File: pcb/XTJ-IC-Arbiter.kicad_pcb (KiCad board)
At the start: 2 copper layers, 82.1 x 48.1 mm, 33 parts, among them J3 DTM13-12PA-R008, SW2 SW_DIP_x02, U1 LM2672N-5.0, U3 Teensy4.0, U4 MCP2562-H-P, U5 SP723ABG

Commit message: 3.3v conn
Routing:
- net 3v3: track 9.27 -> 53.9 mm
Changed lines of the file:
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@@
       (net 4 "can+") (pinfunction "12") (pintype "passive"))
     (model "${KIPRJMOD}/parts/DTM13/DTM13-12PA-R008.step"
-      (offset (xyz 0.635 -30.48 8.255))
+      (offset (xyz 0 -30.48 8.255))
       (scale (xyz 1 1 1))
       (rotate (xyz -90 0 0))
@@
   (segment (start 103.9638 106.7292) (end 103.9638 105.021384) (width 0.1524) (layer "F.Cu") (net 17))
   (segment (start 91.821 108.585) (end 89.027 111.379) (width 0.5) (layer "F.Cu") (net 18))
+  (segment (start 93.8038 105.798616) (end 93.8038 105.021384) (width 0.1524) (layer "F.Cu") (net 20))
+  (segment (start 119.2038 104.4718) (end 120.142 105.41) (width 0.1524) (layer "F.Cu") (net 20))
+  (segment (start 91.458813 112.306) (end 92.437187 112.306) (width 0.1524) (layer "F.Cu") (net 20))
+  (segment (start 87.628 114.504) (end 90.767 111.365) (width 0.1524) (layer "F.Cu") (net 20))
+  (segment (start 110.4498 106.3482) (end 111.5838 105.2142) (width 0.1524) (layer "F.Cu") (net 20))
+  (segment (start 92.437187 112.306) (end 94.71 110.033187) (width 0.1524) (layer "F.Cu") (net 20))
+  (segment (start 112.133384 104.4718) (end 119.2038 104.4718) (width 0.1524) (layer "F.Cu") (net 20))
+  (segment (start 94.665784 104.1594) (end 108.2896 104.1594) (width 0.1524) (layer "F.Cu") (net 20))
   (segment (start 117.71 113.646) (end 117.729 113.665) (width 0.1524) (layer "F.Cu") (net 20))
+  (segment (start 108.2896 104.1594) (end 109.0438 104.9136) (width 0.1524) (layer "F.Cu") (net 20))
+  (segment (start 90.767 111.614187) (end 91.458813 112.306) (width 0.1524) (layer "F.Cu") (net 20))
+  (segment (start 94.71 110.033187) (end 94.71 106.704816) (width 0.1524) (layer "F.Cu") (net 20))
+  (segment (start 111.5838 105.2142) (end 111.5838 105.021384) (width 0.1524) (layer "F.Cu") (net 20))
+  (segment (start 111.5838 105.021384) (end 112.133384 104.4718) (width 0.1524) (layer "F.Cu") (net 20))
+  (segment (start 109.0438 105.798616) (end 109.593384 106.3482) (width 0.1524) (layer "F.Cu") (net 20))
+  (segment (start 90.767 111.365) (end 90.767 111.614187) (width 0.1524) (layer "F.Cu") (net 20))
+  (segment (start 94.71 106.704816) (end 93.8038 105.798616) (width 0.1524) (layer "F.Cu") (net 20))
+  (segment (start 109.593384 106.3482) (end 110.4498 106.3482) (width 0.1524) (layer "F.Cu") (net 20))
   (segment (start 117.71 110.838) (end 117.71 113.646) (width 0.1524) (layer "F.Cu") (net 20))
+  (segment (start 93.8038 105.021384) (end 94.665784 104.1594) (width 0.1524) (layer "F.Cu") (net 20))
+  (segment (start 109.0438 104.9136) (end 109.0438 105.798616) (width 0.1524) (layer "F.Cu") (net 20))
   (segment (start 120.142 108.406) (end 120.142 105.41) (width 0.1524) (layer "B.Cu") (net 20))
   (segment (start 117.71 110.838) (end 120.142 108.406) (width 0.1524) (layer "B.Cu") (net 20))

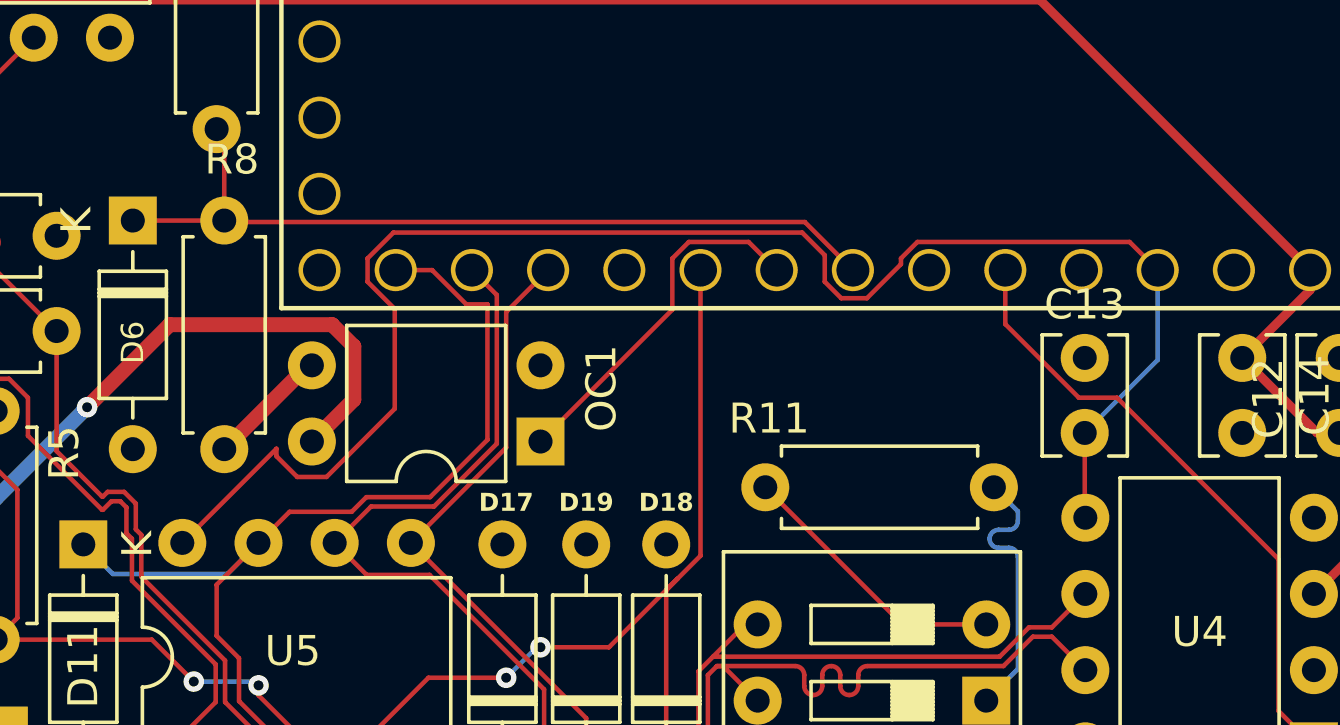
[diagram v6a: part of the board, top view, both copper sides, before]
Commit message: safer 3.3v trace
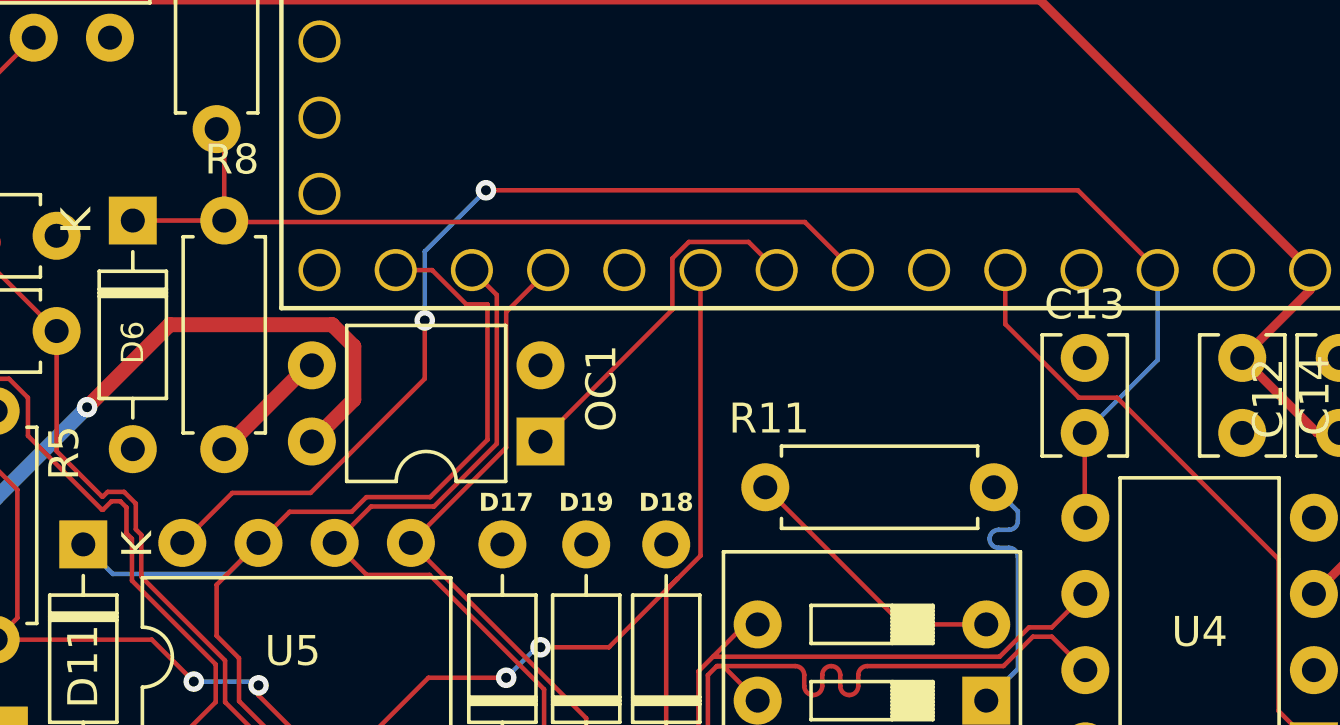
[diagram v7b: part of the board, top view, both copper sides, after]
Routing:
- net 3v3: track 53.9 -> 50.2 mm, vias 0 -> 2
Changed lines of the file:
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@@
     (pad_to_mask_clearance 0.0508)
     (solder_mask_min_width 0.1016)
-    (grid_origin 60.96 100.838)
     (pcbplotparams
       (layerselection 0x00010f0_ffffffff)
@@
   (segment (start 103.9638 106.7292) (end 103.9638 105.021384) (width 0.1524) (layer "F.Cu") (net 17))
   (segment (start 91.821 108.585) (end 89.027 111.379) (width 0.5) (layer "F.Cu") (net 18))
-  (segment (start 93.8038 105.798616) (end 93.8038 105.021384) (width 0.1524) (layer "F.Cu") (net 20))
-  (segment (start 119.2038 104.4718) (end 120.142 105.41) (width 0.1524) (layer "F.Cu") (net 20))
-  (segment (start 91.458813 112.306) (end 92.437187 112.306) (width 0.1524) (layer "F.Cu") (net 20))
-  (segment (start 87.628 114.504) (end 90.767 111.365) (width 0.1524) (layer "F.Cu") (net 20))
-  (segment (start 110.4498 106.3482) (end 111.5838 105.2142) (width 0.1524) (layer "F.Cu") (net 20))
-  (segment (start 92.437187 112.306) (end 94.71 110.033187) (width 0.1524) (layer "F.Cu") (net 20))
-  (segment (start 112.133384 104.4718) (end 119.2038 104.4718) (width 0.1524) (layer "F.Cu") (net 20))
-  (segment (start 94.665784 104.1594) (end 108.2896 104.1594) (width 0.1524) (layer "F.Cu") (net 20))
+  (segment (start 117.482 102.75) (end 120.142 105.41) (width 0.1524) (layer "F.Cu") (net 20))
   (segment (start 117.71 113.646) (end 117.729 113.665) (width 0.1524) (layer "F.Cu") (net 20))
-  (segment (start 108.2896 104.1594) (end 109.0438 104.9136) (width 0.1524) (layer "F.Cu") (net 20))
-  (segment (start 90.767 111.614187) (end 91.458813 112.306) (width 0.1524) (layer "F.Cu") (net 20))
-  (segment (start 94.71 110.033187) (end 94.71 106.704816) (width 0.1524) (layer "F.Cu") (net 20))
-  (segment (start 111.5838 105.2142) (end 111.5838 105.021384) (width 0.1524) (layer "F.Cu") (net 20))
-  (segment (start 111.5838 105.021384) (end 112.133384 104.4718) (width 0.1524) (layer "F.Cu") (net 20))
-  (segment (start 109.0438 105.798616) (end 109.593384 106.3482) (width 0.1524) (layer "F.Cu") (net 20))
-  (segment (start 90.767 111.365) (end 90.767 111.614187) (width 0.1524) (layer "F.Cu") (net 20))
-  (segment (start 94.71 106.704816) (end 93.8038 105.798616) (width 0.1524) (layer "F.Cu") (net 20))
-  (segment (start 109.593384 106.3482) (end 110.4498 106.3482) (width 0.1524) (layer "F.Cu") (net 20))
+  (segment (start 91.905187 112.838) (end 95.71 109.033187) (width 0.1524) (layer "F.Cu") (net 20))
+  (segment (start 95.71 109.033187) (end 95.71 107.088) (width 0.1524) (layer "F.Cu") (net 20))
+  (segment (start 97.75 102.75) (end 117.482 102.75) (width 0.1524) (layer "F.Cu") (net 20))
+  (segment (start 89.294 112.838) (end 91.905187 112.838) (width 0.1524) (layer "F.Cu") (net 20))
   (segment (start 117.71 110.838) (end 117.71 113.646) (width 0.1524) (layer "F.Cu") (net 20))
-  (segment (start 93.8038 105.021384) (end 94.665784 104.1594) (width 0.1524) (layer "F.Cu") (net 20))
-  (segment (start 109.0438 104.9136) (end 109.0438 105.798616) (width 0.1524) (layer "F.Cu") (net 20))
+  (segment (start 87.628 114.504) (end 89.294 112.838) (width 0.1524) (layer "F.Cu") (net 20))
+  (via (at 95.71 107.088) (size 0.6858) (drill 0.3302) (layers "F.Cu" "B.Cu") (net 20))
+  (via (at 97.75 102.75) (size 0.6858) (drill 0.3302) (layers "F.Cu" "B.Cu") (net 20))
   (segment (start 120.142 108.406) (end 120.142 105.41) (width 0.1524) (layer "B.Cu") (net 20))
+  (segment (start 95.71 104.79) (end 97.75 102.75) (width 0.1524) (layer "B.Cu") (net 20))
+  (segment (start 95.71 107.088) (end 95.71 104.79) (width 0.1524) (layer "B.Cu") (net 20))
   (segment (start 117.71 110.838) (end 120.142 108.406) (width 0.1524) (layer "B.Cu") (net 20))
   (segment (start 77.978 117.729) (end 77.978 121.453597) (width 0.3) (layer "F.Cu") (net 21))

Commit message: drc fixes
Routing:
- net can_rx: track 0.00 -> 12.1 mm
- net +5V: track 121.1 -> 120.3 mm
- net 3v3: track 50.2 -> 50.8 mm
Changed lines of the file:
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@@
     (property "Sheetname" "")
     (attr through_hole)
-    (fp_text reference "C13" (at 4.278 0) (layer "F.SilkS")
+    (fp_text reference "C13" (at 2.088 -2.46 90) (layer "F.SilkS")
         (effects (font (size 1 1) (thickness 0.15)))
     )
@@
     (property "Sheetname" "")
     (attr through_hole)
-    (fp_text reference "C12" (at 1.3516 2.3876 90) (layer "F.SilkS")
+    (fp_text reference "C12" (at 0.412 -2.54 90) (layer "F.SilkS")
         (effects (font (size 1 1) (thickness 0.15)))
     )
-    (fp_text value "0.1uf" (at 1.25 2.55 90) (layer "F.Fab")
+    (fp_text value "0.1uf" (at 0.3104 -2.3776 90) (layer "F.Fab")
         (effects (font (size 1 1) (thickness 0.15)))
     )
@@
     (property "Sheetname" "")
     (attr through_hole)
-    (fp_text reference "C14" (at 1.25 -2.413 90) (layer "F.SilkS")
+    (fp_text reference "C14" (at 0.412 2.297 90) (layer "F.SilkS")
         (effects (font (size 1 1) (thickness 0.15)))
     )
@@
   (segment (start 115.062 107.211977) (end 115.062 105.41) (width 0.1524) (layer "F.Cu") (net 8))
   (segment (start 124.168 120.104) (end 124.168 115.046) (width 0.1524) (layer "F.Cu") (net 8))
+  (segment (start 125.349 113.665) (end 124.21763 113.665) (width 0.1524) (layer "F.Cu") (net 9))
+  (segment (start 118.7862 106.5942) (end 117.602 105.41) (width 0.1524) (layer "F.Cu") (net 9))
+  (segment (start 124.21763 113.665) (end 118.7862 108.23357) (width 0.1524) (layer "F.Cu") (net 9))
+  (segment (start 118.7862 108.23357) (end 118.7862 106.5942) (width 0.1524) (layer "F.Cu") (net 9))
   (segment (start 63.49 90.688) (end 63.49 95.681) (width 0.1524) (layer "F.Cu") (net 10))
   (segment (start 63.49 95.681) (end 72.771 104.962) (width 0.1524) (layer "F.Cu") (net 10))
@@
   (segment (start 66.421 90.043) (end 72.7848 96.4068) (width 0.3) (layer "F.Cu") (net 16))
   (segment (start 62.2352 105.6692) (end 62.2352 97.0532) (width 0.3) (layer "F.Cu") (net 16))
-  (segment (start 125.46 110.838) (end 126.21 110.838) (width 0.3) (layer "F.Cu") (net 16))
   (segment (start 116.2188 96.4068) (end 125.222 105.41) (width 0.3) (layer "F.Cu") (net 16))
   (segment (start 57.404 89.154) (end 55.87 90.688) (width 0.3) (layer "F.Cu") (net 16))
@@
   (segment (start 91.821 108.585) (end 89.027 111.379) (width 0.5) (layer "F.Cu") (net 18))
   (segment (start 117.482 102.75) (end 120.142 105.41) (width 0.1524) (layer "F.Cu") (net 20))
+  (segment (start 92.912 112.838) (end 95.71 110.04) (width 0.1524) (layer "F.Cu") (net 20))
+  (segment (start 87.628 114.504) (end 89.294 112.838) (width 0.1524) (layer "F.Cu") (net 20))
   (segment (start 117.71 113.646) (end 117.729 113.665) (width 0.1524) (layer "F.Cu") (net 20))
-  (segment (start 91.905187 112.838) (end 95.71 109.033187) (width 0.1524) (layer "F.Cu") (net 20))
-  (segment (start 95.71 109.033187) (end 95.71 107.088) (width 0.1524) (layer "F.Cu") (net 20))
+  (segment (start 95.71 110.04) (end 95.71 107.088) (width 0.1524) (layer "F.Cu") (net 20))
   (segment (start 97.75 102.75) (end 117.482 102.75) (width 0.1524) (layer "F.Cu") (net 20))
-  (segment (start 89.294 112.838) (end 91.905187 112.838) (width 0.1524) (layer "F.Cu") (net 20))
   (segment (start 117.71 110.838) (end 117.71 113.646) (width 0.1524) (layer "F.Cu") (net 20))
-  (segment (start 87.628 114.504) (end 89.294 112.838) (width 0.1524) (layer "F.Cu") (net 20))
+  (segment (start 89.294 112.838) (end 92.912 112.838) (width 0.1524) (layer "F.Cu") (net 20))
   (via (at 95.71 107.088) (size 0.6858) (drill 0.3302) (layers "F.Cu" "B.Cu") (net 20))
   (via (at 97.75 102.75) (size 0.6858) (drill 0.3302) (layers "F.Cu" "B.Cu") (net 20))
